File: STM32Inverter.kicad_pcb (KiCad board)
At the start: 4 copper layers, 100 x 100 mm, 153 parts, among them J1 STLINK, J2 CURRENT SENSE, J5 UART, J6 INTERFACE, J7 POWER, J8 501571-2007, J9 RESOLVER, Q1 BCX54, Q2 BCX55, Q4 ST3422A, Q5 BCX54, Q6 BCX55, U1 STM32F303VCTx, U10 ULN2002, U11 LM393, U12 LM393, U2 LM358, U3 AD2S1205, U4 74HCT00, U5 74HCT04, U6 74HCT08, U7 MCP2551-I-SN, U8 74HCT08, U9 74HCT08, Y2 CSTNE8M00GH5C000R0, Y3 CSTNE8M00GH5C000R0

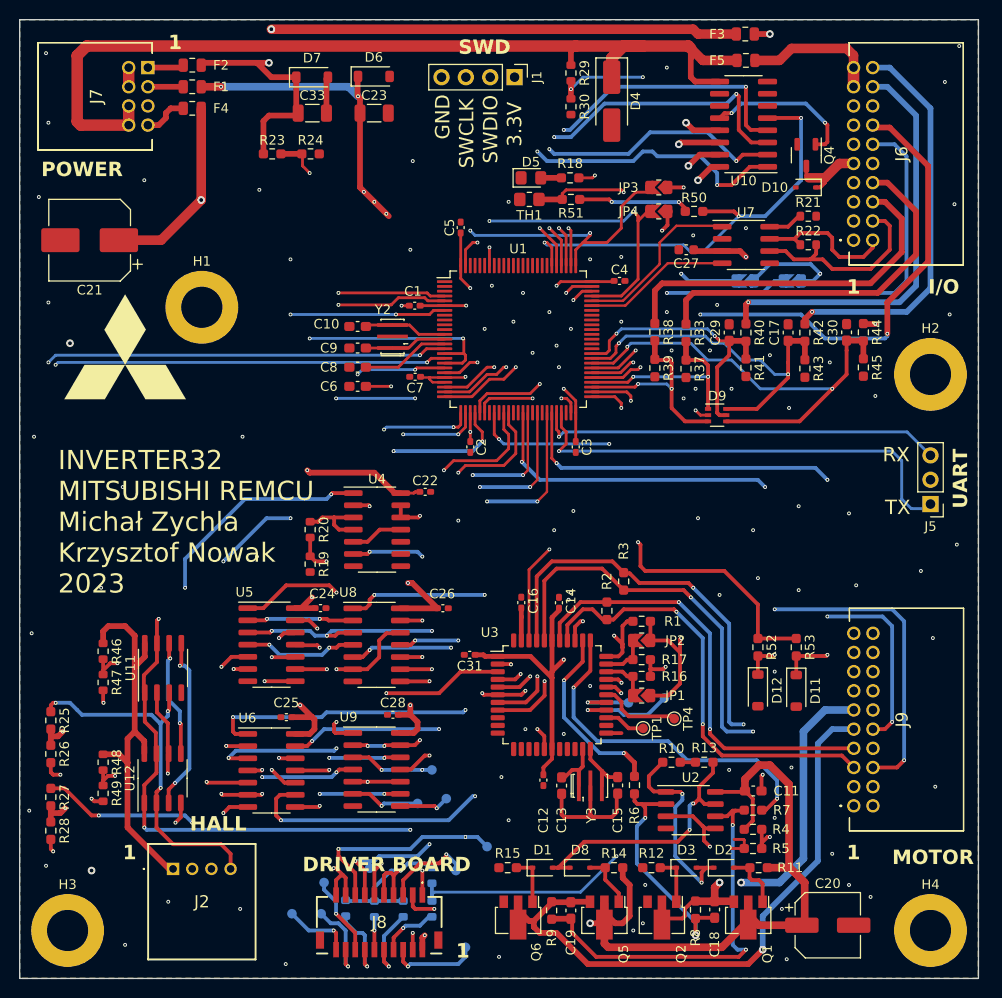
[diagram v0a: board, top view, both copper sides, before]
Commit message: change holes
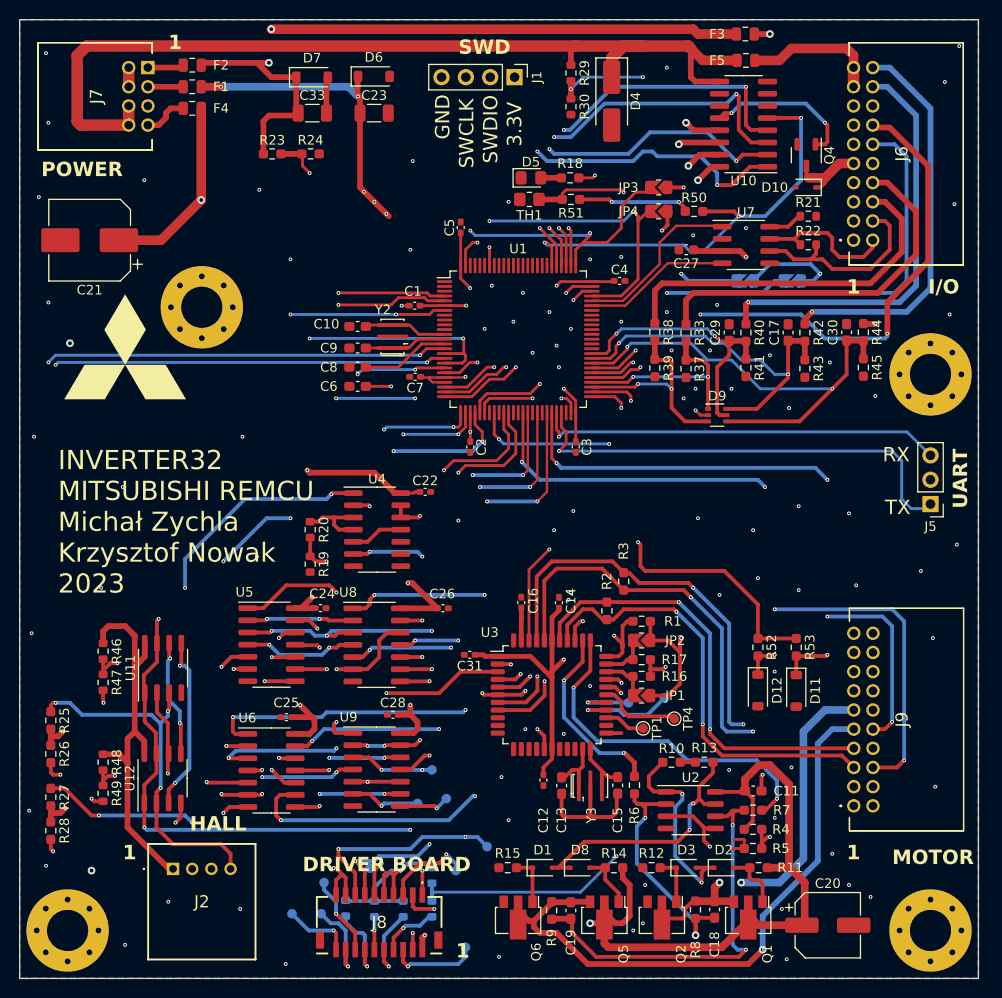
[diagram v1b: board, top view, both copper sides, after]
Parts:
- H1: value M4 -> MountingHole_Pad; footprint MountingHole:MountingHole_4.3mm_M4_ISO7380_Pad -> MountingHole:MountingHole_4.3mm_M4_Pad_Via
- H2, H3, H4: footprint MountingHole:MountingHole_4.3mm_M4_ISO7380_Pad -> MountingHole:MountingHole_4.3mm_M4_Pad_Via

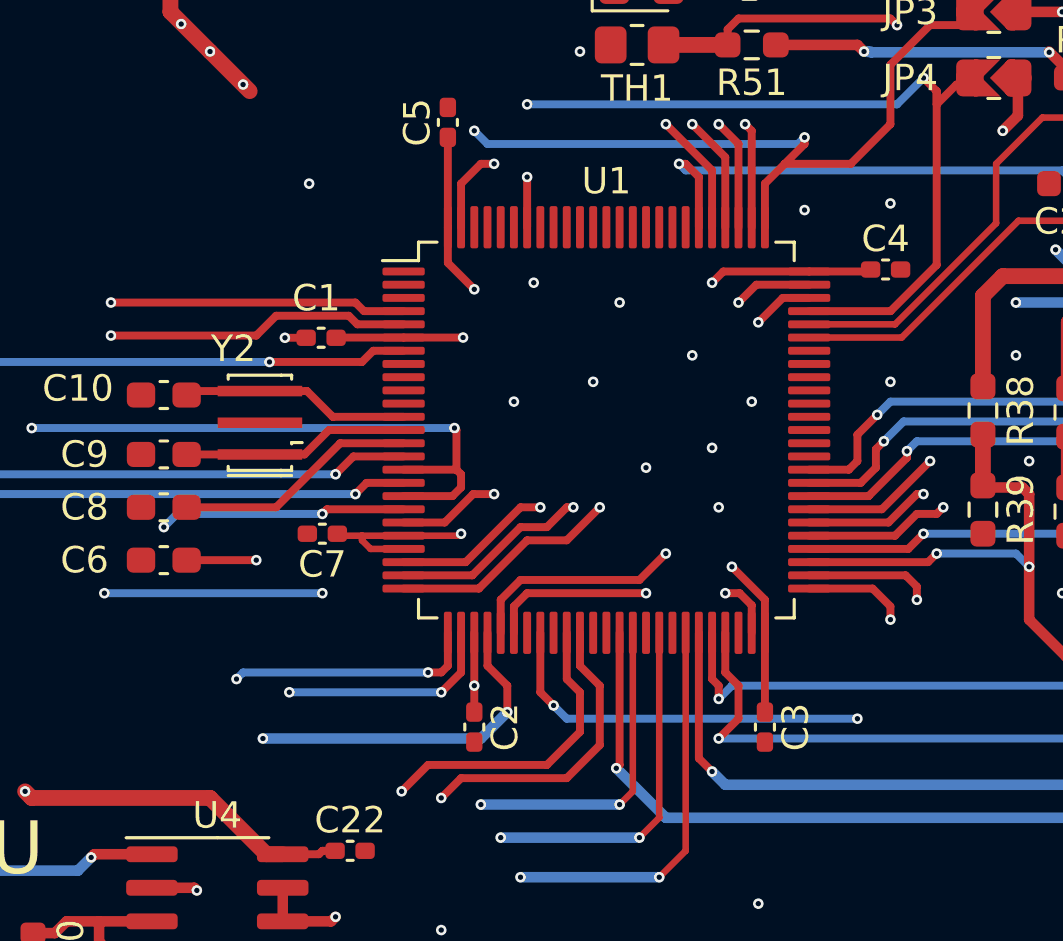
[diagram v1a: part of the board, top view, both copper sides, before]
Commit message: Move T1-3 from ADC1 to ADC2\nNow ADC1 is used only for current measurment
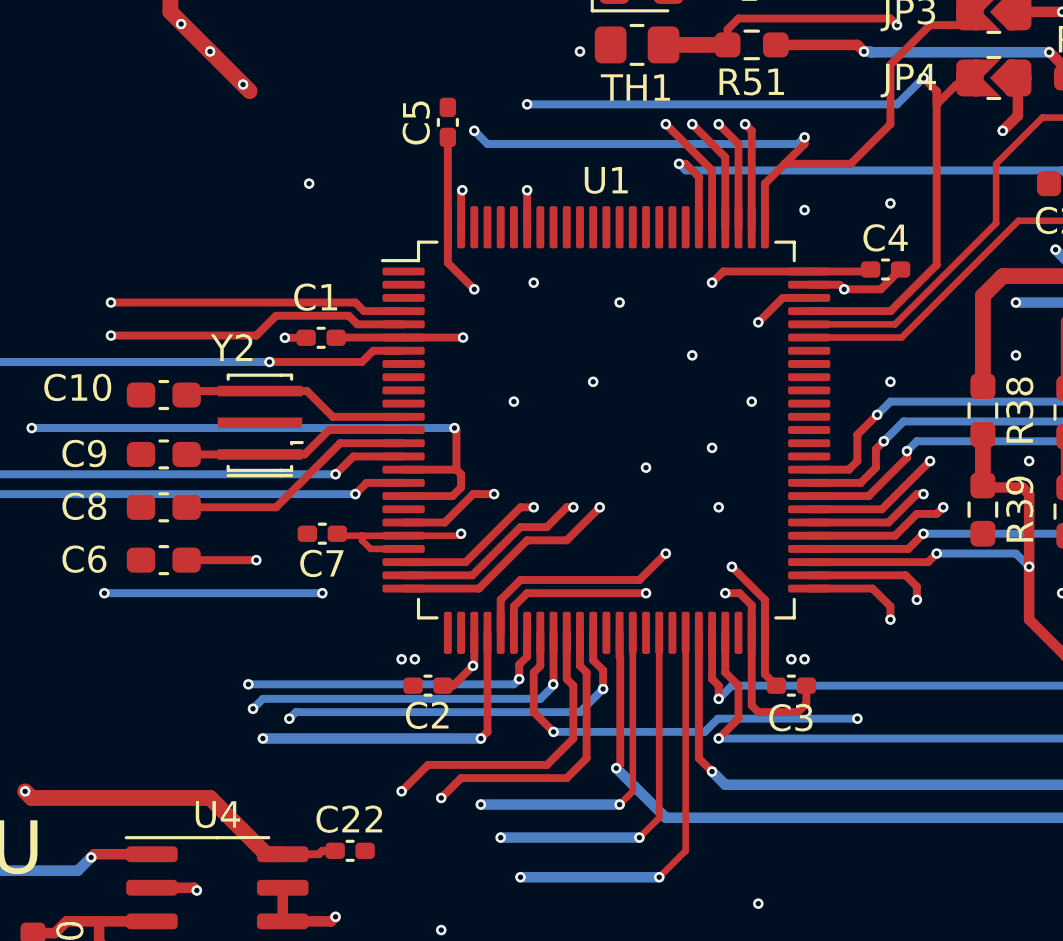
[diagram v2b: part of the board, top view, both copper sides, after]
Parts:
- moved C2 2.35 mm to (57.2, 55.0), turned to 180 degrees
- moved C3 1.86 mm to (71.0, 55.0), turned to 0 degrees
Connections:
- U1 pad 19: /T3_DRV -> unconnected-(U1-PF2-Pad19)
- U1 pad 26: /T2_DRV -> unconnected-(U1-PA3-Pad26)
- U1 pad 27: /T1_DRV -> unconnected-(U1-PF4-Pad27)
- U1 pad 32: unconnected-(U1-PA7-Pad32) -> /T3_DRV
- U1 pad 34: unconnected-(U1-PC5-Pad34) -> /T2_DRV
- U1 pad 37: unconnected-(U1-PB2-Pad37) -> /T1_DRV
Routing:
- net /T1_DRV: track 72.6 -> 77.9 mm
- net GND: track 110.1 -> 114.4 mm, vias 108 -> 112
- net /T2_DRV: track 65.5 -> 68.9 mm
- net /~{RESET_RES}: track 42.4 -> 43.6 mm
- net +3V3: track 130.8 -> 129.7 mm
- net /CS_RES: track 51.1 -> 50.5 mm
- net /T3_DRV: track 79.9 -> 79.4 mm

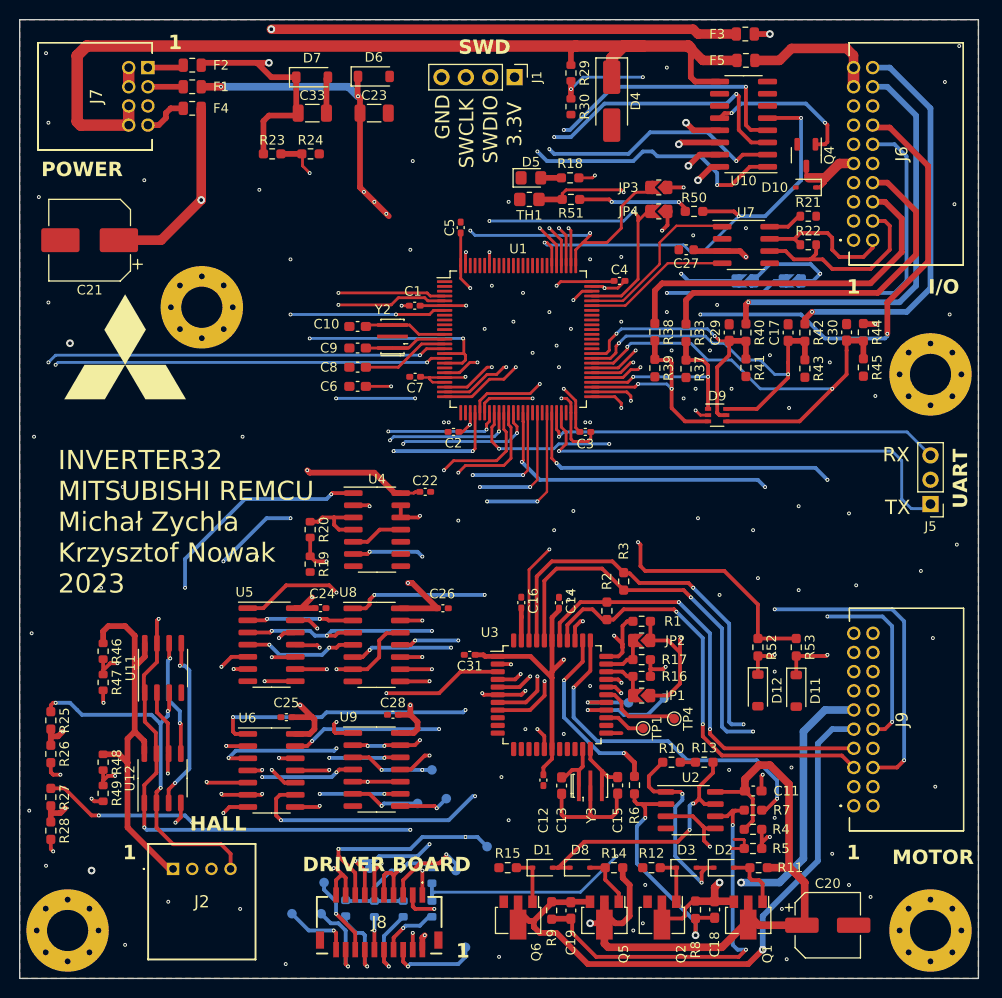
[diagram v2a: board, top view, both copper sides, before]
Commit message: change via size to 0.6/0.3mm
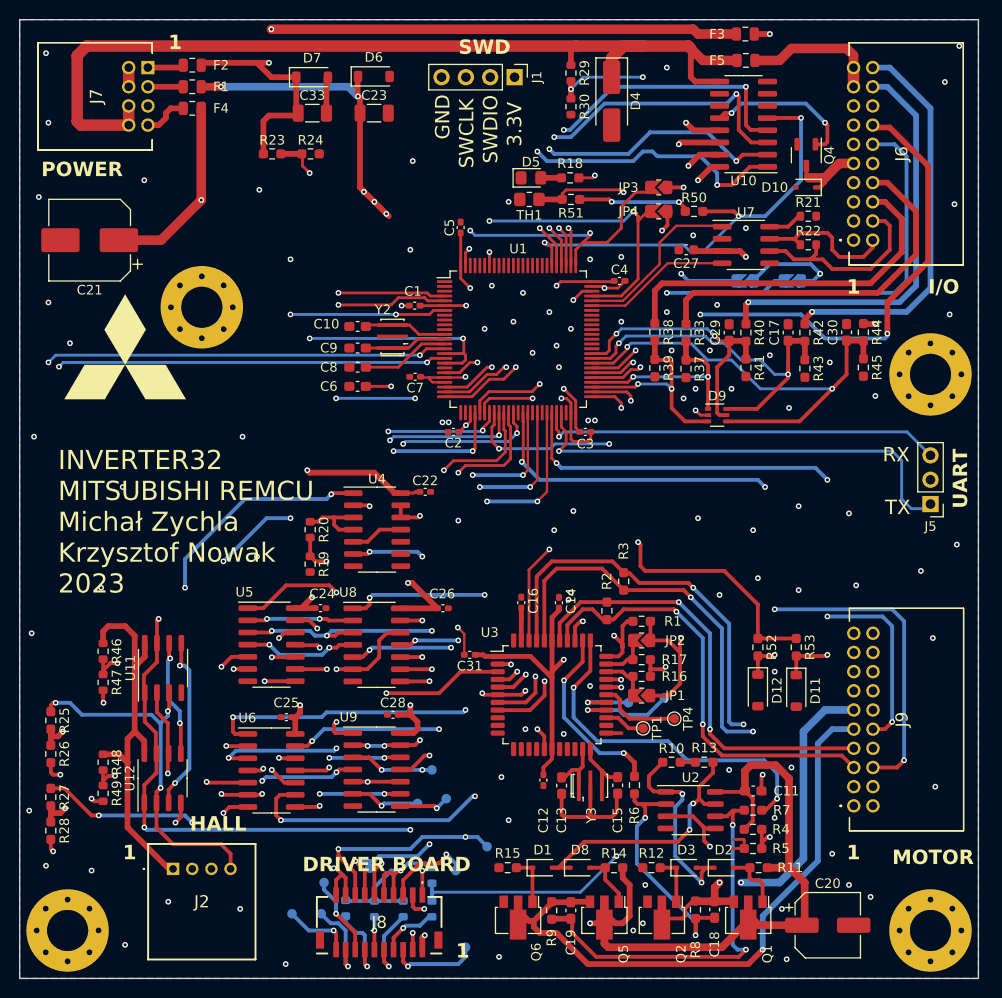
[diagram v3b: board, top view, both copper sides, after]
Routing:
- net +5V: track 209.0 -> 204.8 mm
- net GND: track 114.4 -> 118.1 mm, vias 112 -> 113
- net +15V: track 215.0 -> 215.8 mm
- net /DOS: track 37.5 -> 36.7 mm
- net /SAMPLE: track 42.7 -> 42.1 mm
- net /W_HIGH: track 19.5 -> 18.9 mm
